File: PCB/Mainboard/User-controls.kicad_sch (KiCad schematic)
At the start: 11 parts, among them J2 JST-PH 01x10, J5 JST-PH 01x02, J6 JST-PH 01x02

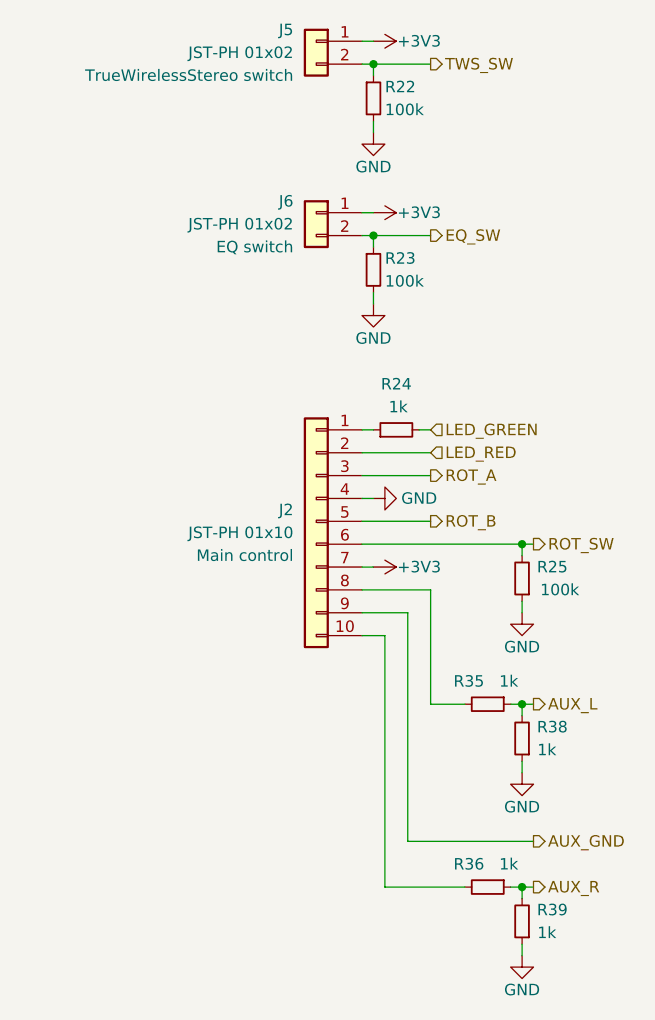
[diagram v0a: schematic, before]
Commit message: Add buck, change some part values
Add new buck in schematic and layout.
Modify BT module footprint,
Change power led resistor from 1k to 100R
Change 4.7u TAS resistors to 10u (consolidation)
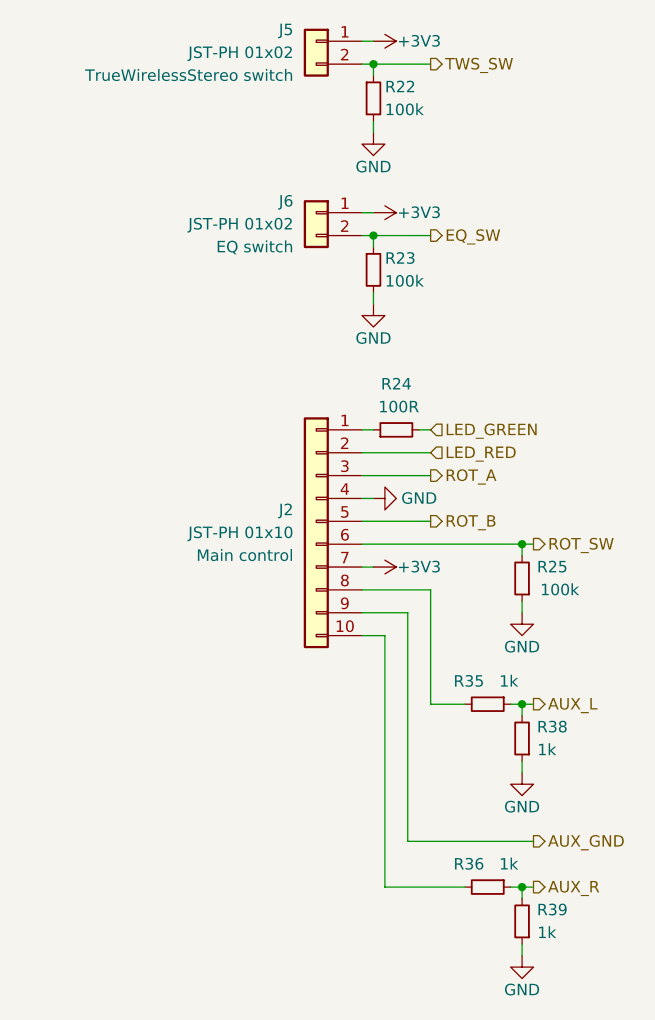
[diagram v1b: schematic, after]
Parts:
- R24: value 1k -> 100R
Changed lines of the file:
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@@
     (in_bom yes) (on_board yes)
     (property "Reference" "R24" (id 0) (at 143.51 88.9 90))
-    (property "Value" "1k" (id 1) (at 144.78 91.44 90)
+    (property "Value" "100R" (id 1) (at 146.05 91.44 90)
       (effects (font (size 1.27 1.27)) (justify left))
     )

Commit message: Mainboard: update symbol fields for bom export
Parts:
- R24: Partnumber RC0603FR-071KL -> RC0603FR-07100RL
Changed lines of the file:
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@@
       (effects (font (size 1.27 1.27)) hide)
     )
-    (property "Partnumber" "RC0603FR-071KL" (id 5) (at 143.51 93.98 0)
+    (property "Partnumber" "RC0603FR-07100RL" (id 5) (at 143.51 93.98 0)
       (effects (font (size 1.27 1.27)) hide)
     )
